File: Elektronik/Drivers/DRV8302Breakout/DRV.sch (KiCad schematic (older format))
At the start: 2 parts

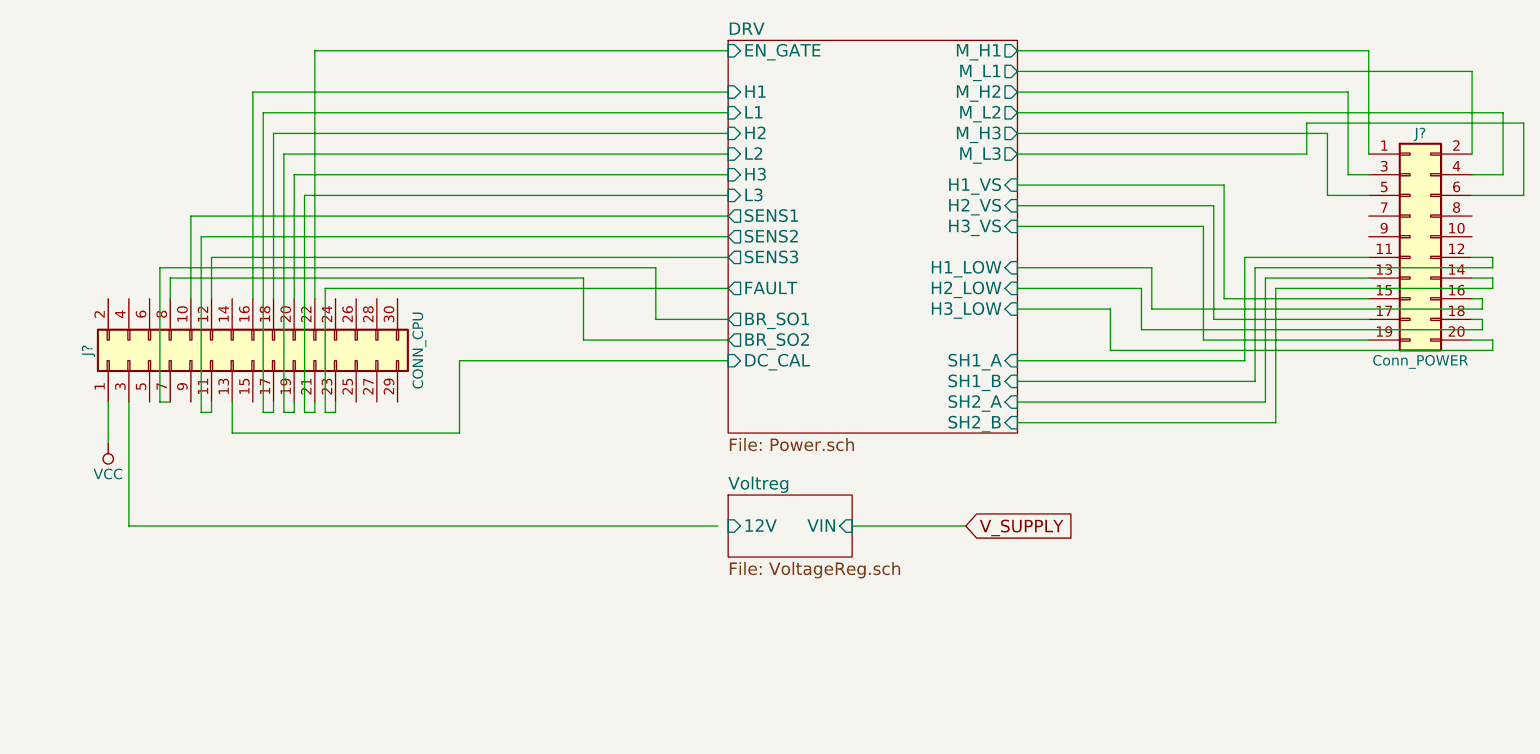
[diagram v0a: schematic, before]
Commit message: first driver pcb most things routed missnig power connector
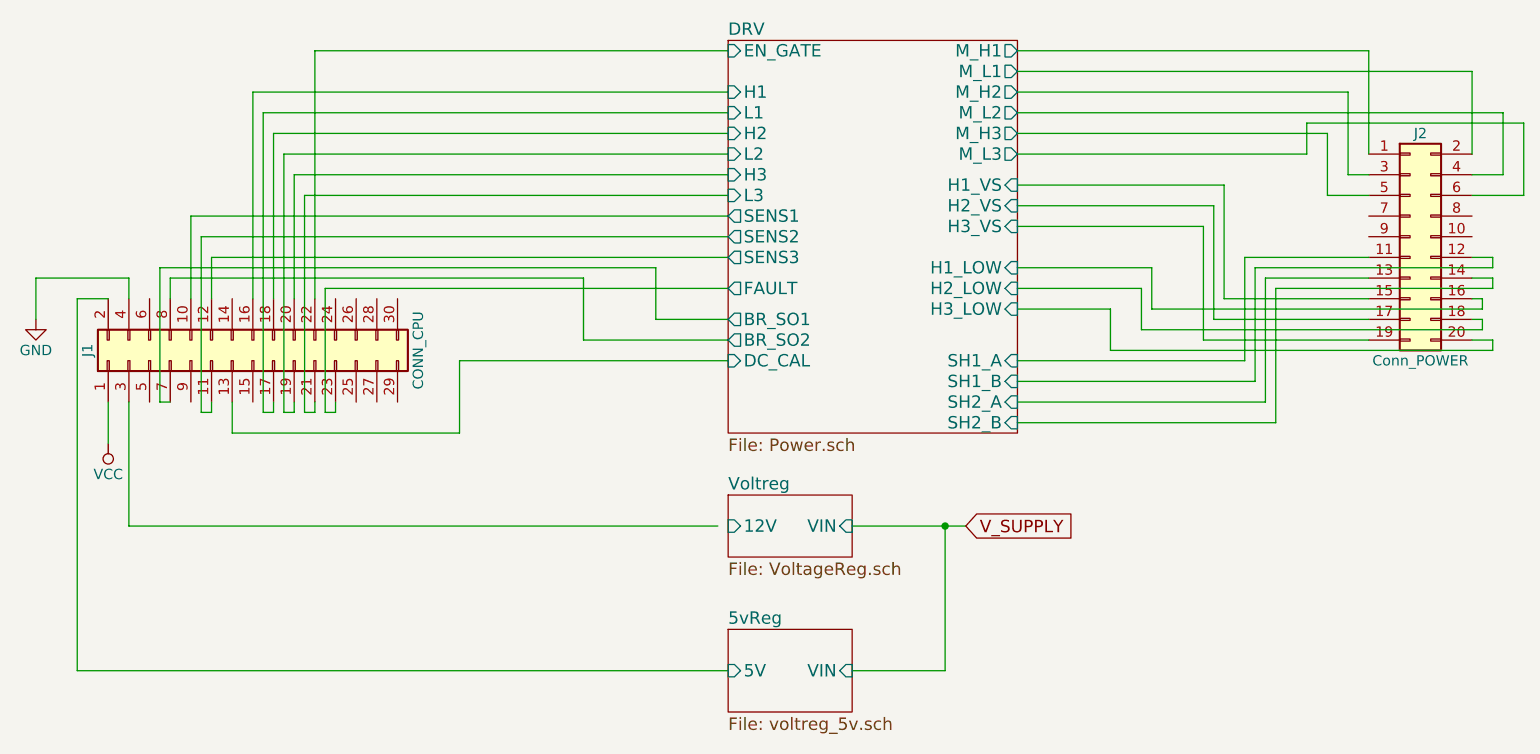
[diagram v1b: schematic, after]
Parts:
- J1: renamed from J?; footprint (none) -> Pin_Headers:Pin_Header_Straight_2x15_Pitch2.54mm
- J2: renamed from J?; footprint (none) -> Pin_Headers:Pin_Header_Straight_2x10_Pitch2.54mm
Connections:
- net 5vReg/5V: now reaches J1.2 (Pin_2)
- net GND: now reaches J1.4 (Pin_4)
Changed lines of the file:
@@
 LIBS:contrib
 LIBS:valves
+LIBS:BLDC_4-cache
+LIBS:BLDC_4-rescue
+LIBS:DRV8302Breakout-cache
 LIBS:DRV-cache
-LIBS:12VFrom60V-cache
 EELAYER 25 0
 EELAYER END
 $Descr A4 11693 8268
 encoding utf-8
-Sheet 1 3
+Sheet 1 4
 Title ""
 Date ""
@@
 	2900 3100 2900 3050
 $Comp
-L VCC #PWR?
+L VCC #PWR01
 U 1 1 5AFD4E17
 P 1800 3250
-F 0 "#PWR?" H 1800 3100 50  0001 C CNN
+F 0 "#PWR01" H 1800 3100 50  0001 C CNN
 F 1 "VCC" H 1800 3400 50  0000 C CNN
 F 2 "" H 1800 3250 50  0001 C CNN
@@
 	2100 2450 2100 2550
 $Comp
-L Conn_02x15_Odd_Even J?
+L Conn_02x15_Odd_Even J1
 U 1 1 5AFD845E
 P 2500 2850
-F 0 "J?" H 2550 3650 50  0000 C CNN
+F 0 "J1" H 2550 3650 50  0000 C CNN
 F 1 "CONN_CPU" H 2550 2050 50  0000 C CNN
-F 2 "" H 2500 2850 50  0001 C CNN
+F 2 "Pin_Headers:Pin_Header_Straight_2x15_Pitch2.54mm" H 2500 2850 50  0001 C CNN
 F 3 "" H 2500 2850 50  0001 C CNN
 	1    2500 2850
@@
 	2400 3200 2400 3050
 $Comp
-L Conn_02x10_Odd_Even J?
+L Conn_02x10_Odd_Even J2
 U 1 1 5AFDA65D
 P 8100 2250
-F 0 "J?" H 8150 2750 50  0000 C CNN
+F 0 "J2" H 8150 2750 50  0000 C CNN
 F 1 "Conn_POWER" H 8150 1650 50  0000 C CNN
-F 2 "" H 8100 2250 50  0001 C CNN
+F 2 "Pin_Headers:Pin_Header_Straight_2x10_Pitch2.54mm" H 8100 2250 50  0001 C CNN
 F 3 "" H 8100 2250 50  0001 C CNN
 	1    8100 2250
@@
 Wire Wire Line
 	5400 3650 5950 3650
+$Sheet
+S 4800 4150 600  400
+U 5B00867F
+F0 "5vReg" 60
+F1 "voltreg_5v.sch" 60
+F2 "VIN" I R 5400 4350 60
+F3 "5V" I L 4800 4350 60
+$EndSheet
+Wire Wire Line
+	5400 4350 5850 4350
+Wire Wire Line
+	5850 4350 5850 3650
+Connection ~ 5850 3650
+Wire Wire Line
+	4800 4350 1650 4350
+Wire Wire Line
+	1650 4350 1650 2550
+Wire Wire Line
+	1650 2550 1800 2550
+$Comp
+L GND #PWR02
+U 1 1 5B00A548
+P 1450 2650
+F 0 "#PWR02" H 1450 2400 50  0001 C CNN
+F 1 "GND" H 1450 2500 50  0000 C CNN
+F 2 "" H 1450 2650 50  0001 C CNN
+F 3 "" H 1450 2650 50  0001 C CNN
+	1    1450 2650
+	1    0    0    -1
+$EndComp
+Wire Wire Line
+	1900 2550 1900 2450
+Wire Wire Line
+	1900 2450 1450 2450
+Wire Wire Line
+	1450 2450 1450 2650
 $EndSCHEMATC

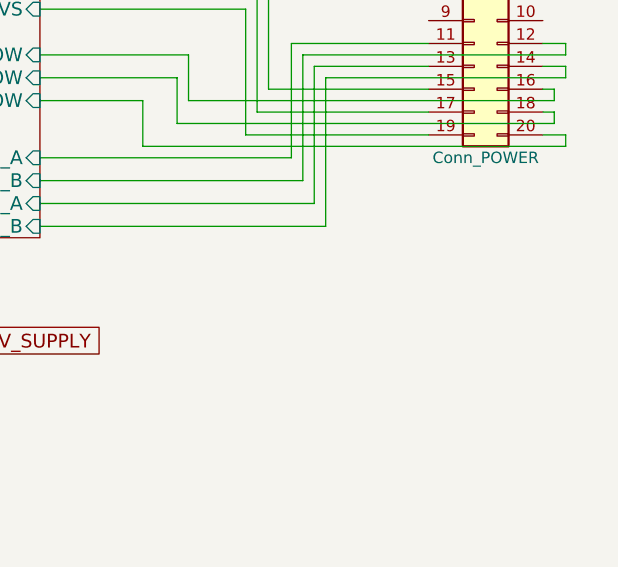
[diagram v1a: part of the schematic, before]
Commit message: added power connection to driver board
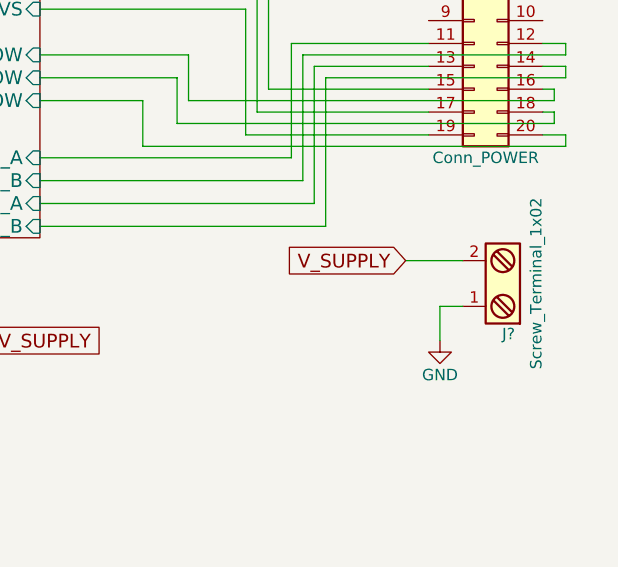
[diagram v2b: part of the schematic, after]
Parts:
- added J?: Screw_Terminal_1x02, symbol Screw_Terminal_1x02
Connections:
- net GND: now also J?.1
- net V_SUPPLY: now also J?.2
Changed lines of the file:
@@
 Wire Wire Line
 	1450 2450 1450 2650
+$Comp
+L Screw_Terminal_1x02 J?
+U 1 1 5B01B291
+P 8250 3400
+F 0 "J?" H 8250 3650 50  0000 C TNN
+F 1 "Screw_Terminal_1x02" V 8100 3400 50  0000 C TNN
+F 2 "" H 8250 3175 50  0001 C CNN
+F 3 "" H 8225 3400 50  0001 C CNN
+	1    8250 3400
+	-1   0    0    1
+$EndComp
+$Comp
+L GND #PWR?
+U 1 1 5B01B3E6
+P 7950 3650
+F 0 "#PWR?" H 7950 3400 50  0001 C CNN
+F 1 "GND" H 7950 3500 50  0000 C CNN
+F 2 "" H 7950 3650 50  0001 C CNN
+F 3 "" H 7950 3650 50  0001 C CNN
+	1    7950 3650
+	1    0    0    -1
+$EndComp
+Text GLabel 7800 3300 0    60   Input ~ 0
+V_SUPPLY
+Wire Wire Line
+	8050 3300 7800 3300
+Wire Wire Line
+	8050 3500 7950 3500
+Wire Wire Line
+	7950 3500 7950 3650
 $EndSCHEMATC
